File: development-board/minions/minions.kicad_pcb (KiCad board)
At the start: 2 copper layers, 150 x 100 mm, 101 parts, among them J1 Pinout, J2 SWD_JLINK, J3 0.91 OLED, J4 BatCon, J5 Pinout, K1 KEYSW, K2 KEYSW, K3 KEYSW, K4 KEYSW, K5 KEYSW, K6 KEYSW, K7 KEYSW, K8 KEYSW, P1 USB_C_Plug_USB2.0, Q1 PJA3404_(G1,D3,S2), Q2 PJA3405_(G1,D3,S2), SW1 RST, SW3 PWR_SWITCH, SW4 5V_EN, U10 MAX17048, U4 CH340C, U5 BQ24075RGT_DPPM, U6 TPS63002_SEPIC_5V, U7 nRF52832-QFxx, U8 MCP23017_SS, U9 TPS63001_SEPIC_3V3, Y1 32MHz_CF4032M00020001

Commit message: feat: routing minions part 1
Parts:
- removed J4: BatCon, Connector_PinHeader_2.54mm:PinHeader_1x02_P2.54mm_Horizontal
- added C10: 1uF, Capacitor_SMD:C_0805_2012Metric_Pad1.18x1.45mm_HandSolder, F.Cu at (212.4, 170.8)
- added C22: 0.1uF, Capacitor_SMD:C_0805_2012Metric_Pad1.18x1.45mm_HandSolder, F.Cu at (153.9, 88.8)
- added J6: ConnBattery, Connector_PinHeader_2.54mm:PinHeader_1x03_P2.54mm_Horizontal, F.Cu at (212.9, 160.4)
- added SW2: SW_RGB, Button_Switch_SMD:SW_SPDT_PCM12, F.Cu at (193.8, 122.5)
- added U1: SN74LV1T34DBV, Package_TO_SOT_SMD:SOT-23-5_HandSoldering, F.Cu at (184.8, 124.4)
- R15, R17: value 1K -> 1K5
- moved J2 93.0 mm to (143.7, 113.2), turned to -90 degrees
- moved J5 89.7 mm to (110.0, 74.8), turned to 0 degrees
- moved C19 81.5 mm to (117.7, 96.8), turned to 0 degrees
- moved C36 75.1 mm to (146.1, 76.3)
- moved C35 75.1 mm to (146.1, 78.4)
- moved R10 75.1 mm to (148.1, 80.8), turned to 0 degrees
- moved SW1 72.5 mm to (117.7, 103.6), turned to -90 degrees
- moved R1 71.9 mm to (126.0, 97.2)
- moved C8 71.5 mm to (140.4, 82.4)
- moved L3 71.2 mm to (135.2, 73.0)
- moved Y1 71.0 mm to (140.5, 78.2)
- moved C18 70.8 mm to (140.5, 74.2)
- moved U8 70.4 mm to (128.8, 106.2)
- moved C56 69.3 mm to (153.9, 86.6), turned to 0 degrees
- moved U10 69.0 mm to (153.8, 91.6)
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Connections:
- C41 pad 1: +5V -> Net-(D11-VDD)
- C42 pad 1: +5V -> Net-(D11-VDD)
- C43 pad 1: +5V -> Net-(D11-VDD)
- C44 pad 1: +5V -> Net-(D11-VDD)
- D11 pad 4: +5V -> Net-(D11-VDD)
- D17 pad 4: +5V -> Net-(D11-VDD)
- D23 pad 4: +5V -> Net-(D11-VDD)
- D32 pad 1: Net-(D32-K) -> /~{CHG}
- D4 pad 1: Net-(D4-K) -> /~{PGOOD}
- D8 pad 3: TX -> Net-(D8-DIN)
- D8 pad 4: +5V -> Net-(D11-VDD)
- J1 pad 1: /P0.24 -> /~{PGOOD}
- J1 pad 2: /P0.25 -> /~{CHG}
- J1 pad 3: /P0.26 -> /~{ALRT}
- U10 pad 5: unconnected-(U10-~{ALRT}-Pad5) -> /~{ALRT}
- U5 pad 1: unconnected-(U5-TS-Pad1) -> /TS
- U5 pad 7: Net-(D4-K) -> /~{PGOOD}
- U5 pad 9: Net-(D32-K) -> /~{CHG}
- U7 pad 29: /P0.24 -> /~{PGOOD}
- U7 pad 37: /P0.25 -> /~{CHG}
- U7 pad 38: /P0.26 -> /~{ALRT}
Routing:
- net GND: track 58.4 -> 169.6 mm
- net /~{PGOOD}: track 0.00 -> 63.0 mm
- net /SWCLK: track 0.00 -> 41.3 mm, vias 0 -> 4
- net Net-(U7-ANT): track 0.00 -> 40.0 mm
- net +3.3V: track 7.37 -> 39.1 mm
- net /P0.31/AIN7: track 0.00 -> 26.6 mm
- net /P0.00/XL1: track 0.00 -> 25.6 mm
- net /P0.30/AIN6: track 0.00 -> 24.1 mm
- net /NFC2/P0.10: track 0.00 -> 24.1 mm
- net /P0.01/XL2: track 0.00 -> 23.8 mm
- net /P0.02/AIN0: track 0.00 -> 22.9 mm
- net /P0.03/AIN1: track 0.00 -> 22.3 mm
- net /NFC1/P0.09: track 0.00 -> 21.9 mm
- net /P0.08: track 0.00 -> 21.8 mm
- net Net-(U7-DEC3): track 0.00 -> 21.8 mm
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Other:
- board outline removed

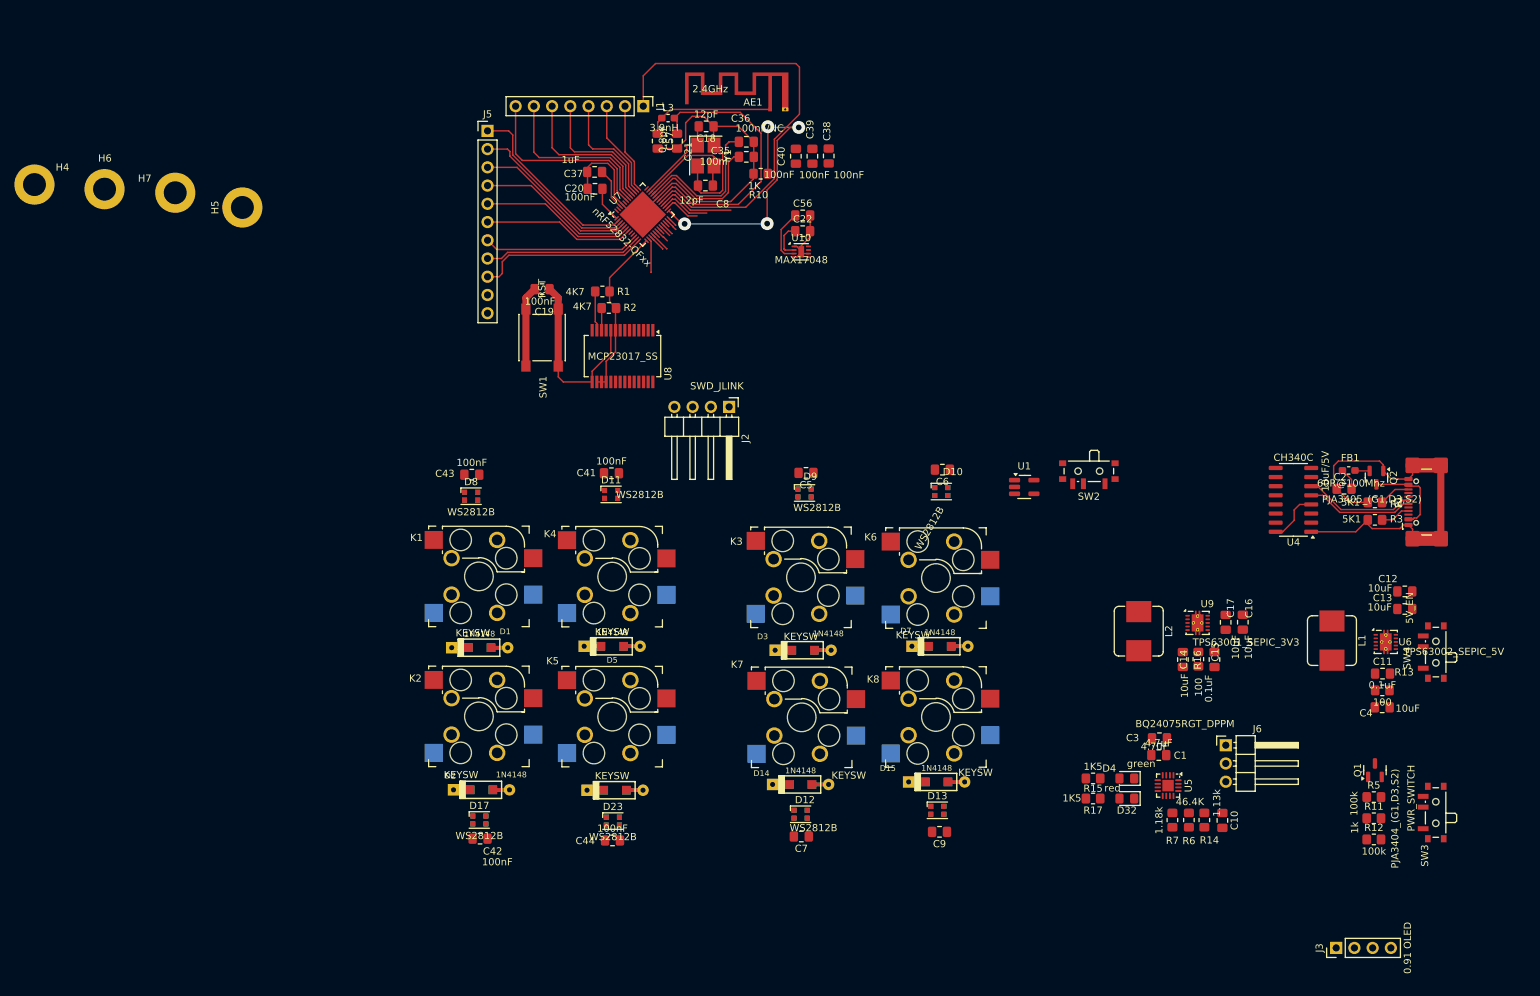
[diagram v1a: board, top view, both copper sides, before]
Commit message: feat: finish routing part 1
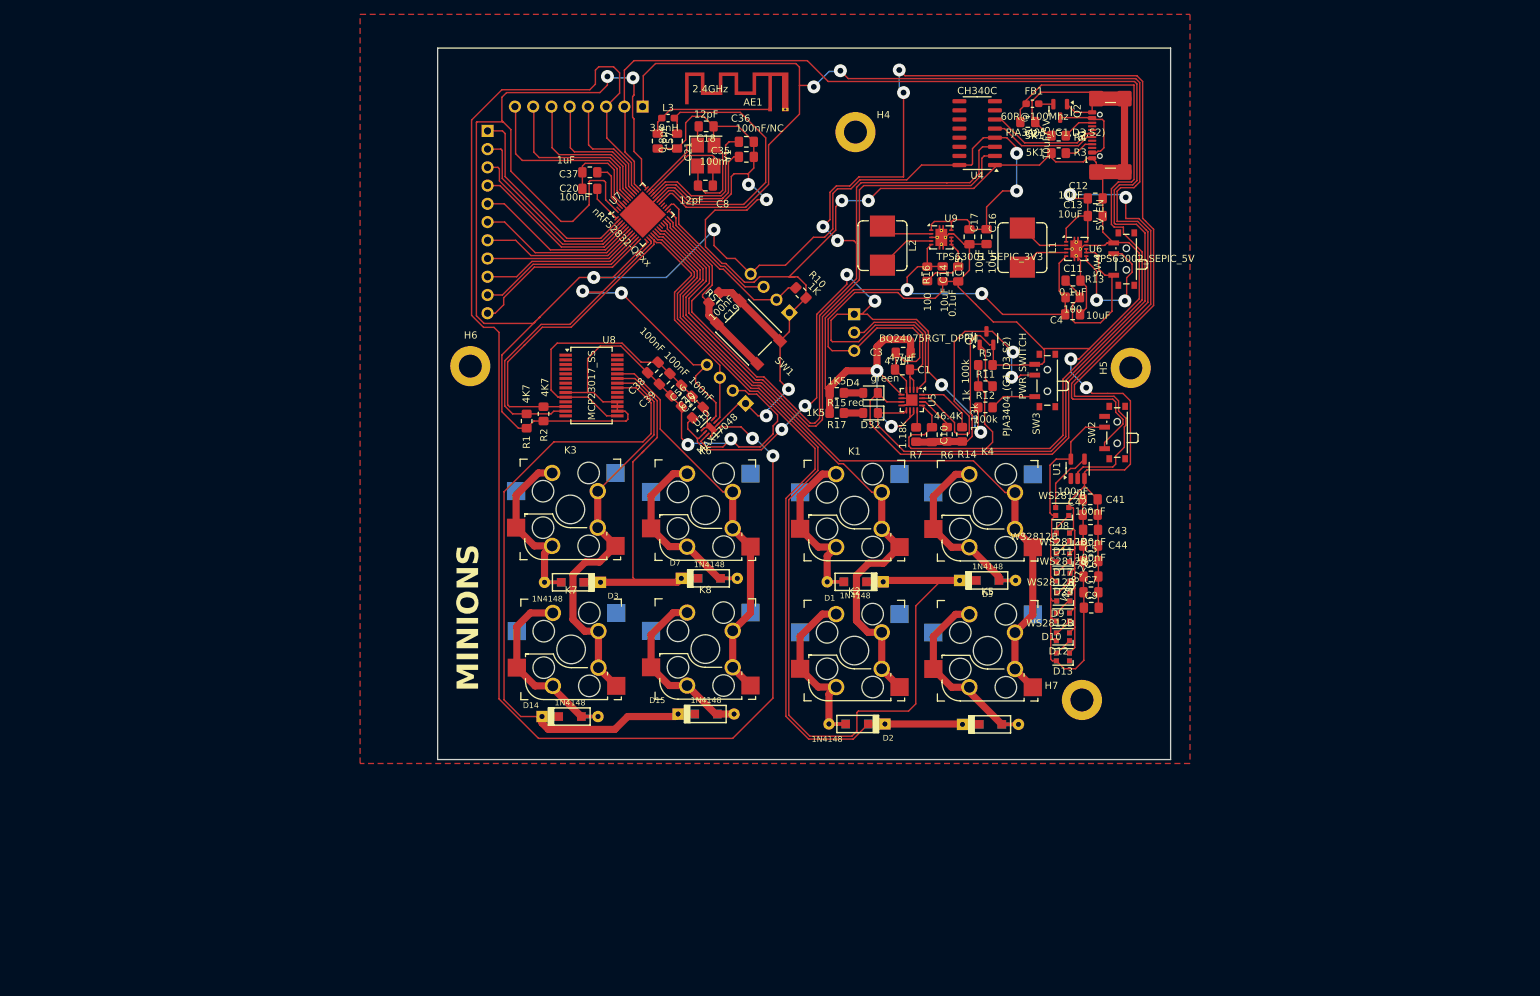
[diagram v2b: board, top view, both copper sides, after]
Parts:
- J1, J3, J5, K1, K2, K3, K4, K5, K6, K7, K8: moved to B.Cu
- J2: footprint Connector_PinHeader_2.54mm:PinHeader_1x04_P2.54mm_Horizontal -> Connector_PinHeader_2.54mm:PinHeader_1x04_P2.54mm_Vertical; moved to B.Cu
- J6: footprint Connector_PinHeader_2.54mm:PinHeader_1x03_P2.54mm_Horizontal -> Connector_PinHeader_2.54mm:PinHeader_1x03_P2.54mm_Vertical; moved to B.Cu
- moved H7 144.7 mm to (192.8, 154.1)
- moved H5 125.8 mm to (199.7, 107.8)
- moved H4 114.6 mm to (161.3, 75.0)
- moved J3 111.9 mm to (146.0, 112.8), turned to 45 degrees
- moved C42 96.2 mm to (194.0, 128.2), turned to 0 degrees
- moved D17 89.1 mm to (190.2, 134.2), turned to 180 degrees
- moved C43 86.5 mm to (194.1, 130.3), turned to 0 degrees
- moved D8 82.4 mm to (190.1, 127.8), turned to 180 degrees
- moved SW3 80.9 mm to (187.7, 109.5)
- moved R5 80.9 mm to (179.4, 107.4)
- moved Q1 80.9 mm to (179.6, 103.6)
- moved R11 80.9 mm to (179.4, 110.3)
- moved R12 80.9 mm to (179.4, 113.3)
- moved J6 79.3 mm to (161.1, 100.3), turned to 180 degrees
- moved C44 78.2 mm to (194.1, 132.6), turned to 0 degrees
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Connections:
- C41 pad 1: Net-(D11-VDD) -> Net-(D10-VDD)
- C42 pad 1: Net-(D11-VDD) -> Net-(D10-VDD)
- C43 pad 1: Net-(D11-VDD) -> Net-(D10-VDD)
- C44 pad 1: Net-(D11-VDD) -> Net-(D10-VDD)
- C5 pad 1: +5V -> Net-(D10-VDD)
- C6 pad 1: +5V -> Net-(D10-VDD)
- C7 pad 1: +5V -> Net-(D10-VDD)
- C9 pad 1: +5V -> Net-(D10-VDD)
- D10 pad 4: +5V -> Net-(D10-VDD)
- D11 pad 4: Net-(D11-VDD) -> Net-(D10-VDD)
- D12 pad 4: +5V -> Net-(D10-VDD)
- D13 pad 4: +5V -> Net-(D10-VDD)
- D17 pad 4: Net-(D11-VDD) -> Net-(D10-VDD)
- D23 pad 4: Net-(D11-VDD) -> Net-(D10-VDD)
- D8 pad 4: Net-(D11-VDD) -> Net-(D10-VDD)
- D9 pad 4: +5V -> Net-(D10-VDD)
- J5 pad 10: /P0.17 -> Net-(J5-Pin_10)
- J5 pad 11: /P0.18/SWO -> Net-(J5-Pin_11)
- J5 pad 7: /P0.08 -> Net-(J5-Pin_7)
- J5 pad 8: /NFC1/P0.09 -> Net-(J5-Pin_8)
- J5 pad 9: /NFC2/P0.10 -> Net-(J5-Pin_9)
- SW2 pad 2: Net-(D11-VDD) -> Net-(D10-VDD)
- U1 pad 5: Net-(D11-VDD) -> Net-(D10-VDD)
- U7 pad 10: /P0.08 -> Net-(J5-Pin_9)
- U7 pad 11: /NFC1/P0.09 -> Net-(J5-Pin_10)
- U7 pad 12: /NFC2/P0.10 -> Net-(J5-Pin_11)
- U7 pad 14: row1 -> SDA
- U7 pad 15: row2 -> SCL
- U7 pad 16: col1 -> row2
- U7 pad 17: col2 -> row1
- U7 pad 18: TX -> col1
- U7 pad 19: RX -> col2
- U7 pad 20: /P0.17 -> unconnected-(U7-P0.17-Pad20)
- U7 pad 21: /P0.18/SWO -> unconnected-(U7-P0.18/SWO-Pad21)
- U7 pad 22: mcp_col1 -> RX
- U7 pad 23: mcp_col2 -> TX
- U7 pad 27: mcp_row1 -> unconnected-(U7-P0.22-Pad27)
- U7 pad 28: mcp_row2 -> unconnected-(U7-P0.23-Pad28)
- U7 pad 8: SCL -> Net-(J5-Pin_7)
- U7 pad 9: SDA -> Net-(J5-Pin_8)
- U8 pad 1: mcp_col1 -> unconnected-(U8-GPB0-Pad1)
- U8 pad 2: mcp_col2 -> unconnected-(U8-GPB1-Pad2)
- U8 pad 21: mcp_row1 -> mcp_row2
- U8 pad 22: mcp_row2 -> mcp_col1
- U8 pad 23: unconnected-(U8-GPA2-Pad23) -> mcp_row1
- U8 pad 24: unconnected-(U8-GPA3-Pad24) -> mcp_col2
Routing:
- net GND: track 169.6 -> 557.1 mm, vias 0 -> 8
- net +3.3V: track 39.1 -> 339.3 mm, vias 0 -> 8
- net TX: track 2.08 -> 242.2 mm, vias 0 -> 4
- net /~{ALRT}: track 13.5 -> 212.7 mm, vias 0 -> 2
- net /~{CHG}: track 12.3 -> 184.6 mm
- net /~{PGOOD}: track 63.0 -> 210.6 mm, vias 0 -> 2
- net row1: track 4.85 -> 135.6 mm
- net VBUS: track 3.07 -> 121.9 mm
- net +BATT: track 5.16 -> 117.5 mm, vias 0 -> 6
- net VDD: track 0.00 -> 106.6 mm, vias 0 -> 4
- net row2: track 2.43 -> 105.6 mm
- net col2: track 0.93 -> 102.2 mm
- net RX: track 1.00 -> 98.1 mm
- net col1: track 2.82 -> 89.1 mm
- net mcp_row2: track 10.9 -> 90.1 mm
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- added copper zone on F.Cu, net +3.3V
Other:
- board outline added: 102.1 x 99.1 mm
- board text added: "MINIONS"
